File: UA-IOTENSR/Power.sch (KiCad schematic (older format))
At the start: 23 parts, among them IC201 BQ2000TPN-B5, J201 ZX62-AB-5PA_31_, J202 S2B-ZR-SM4A-TF(LF)(SN)

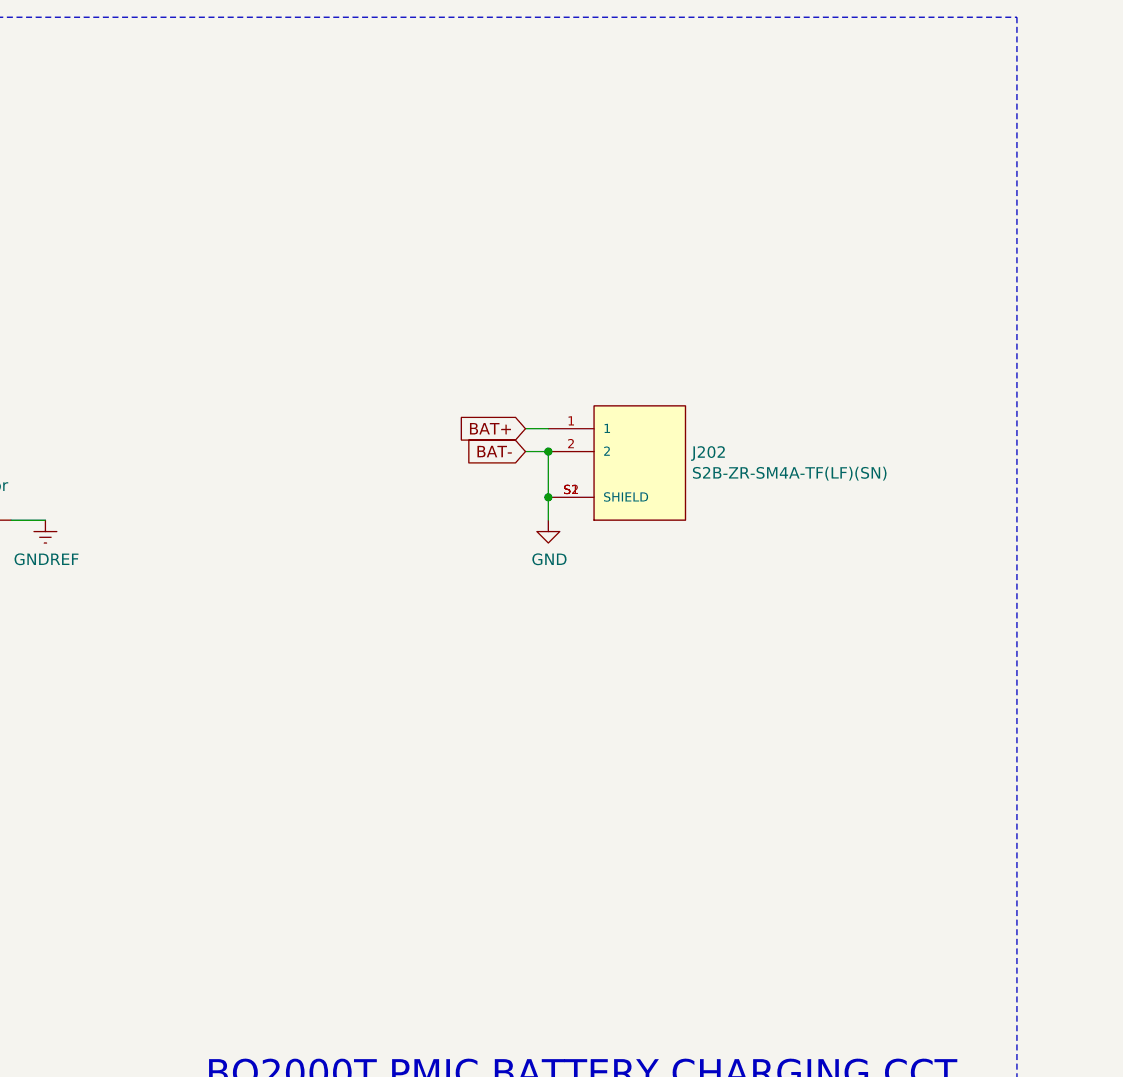
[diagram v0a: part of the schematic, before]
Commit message: Added 3V3 switch reg with footprint
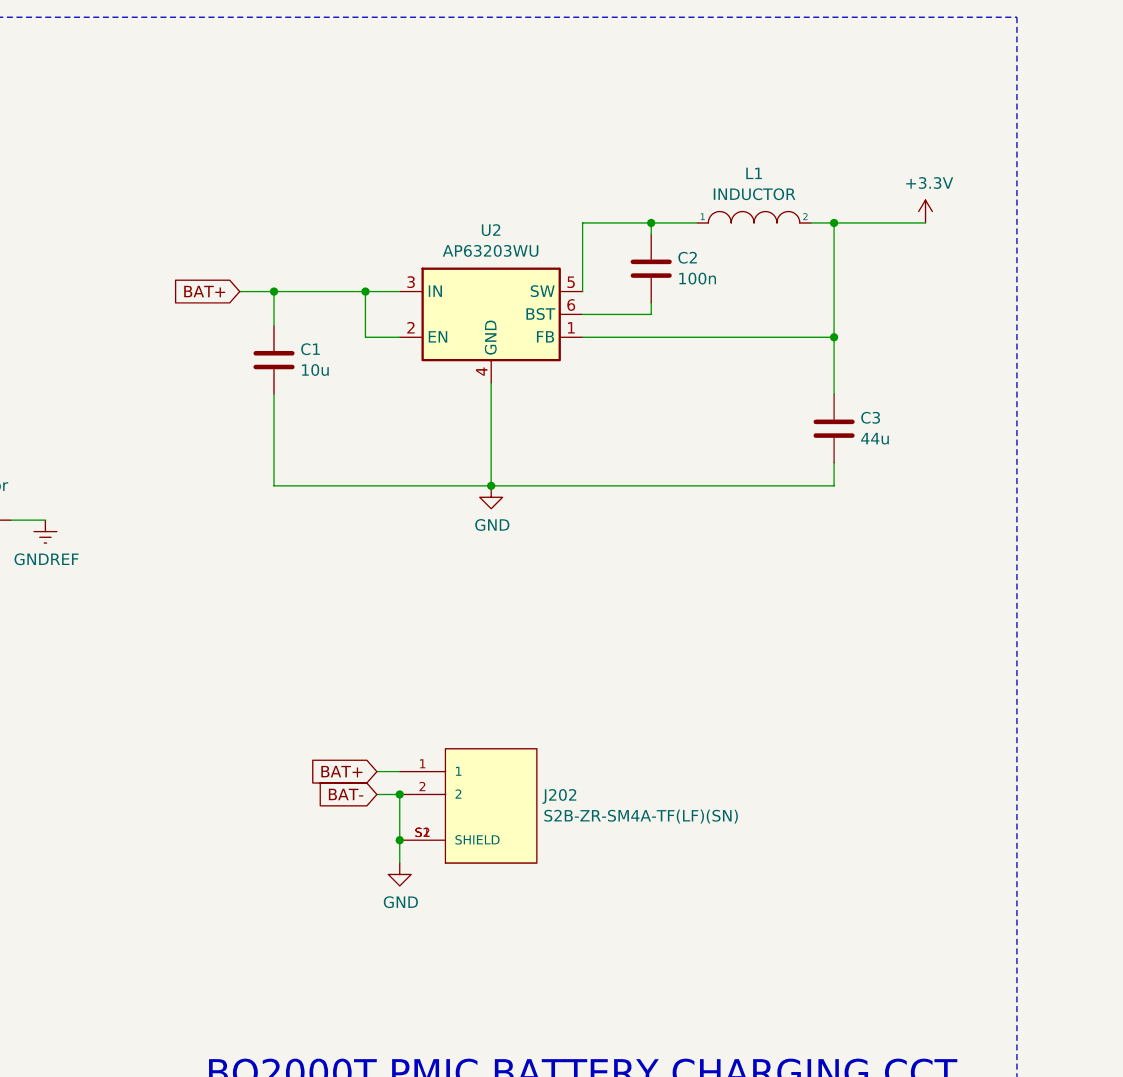
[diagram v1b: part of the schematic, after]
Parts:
- added C1: 10u, Capacitor_SMD:C_0805_2012Metric_Pad1.18x1.45mm_HandSolder, symbol Device:C
- added C2: 100n, Capacitor_SMD:C_0805_2012Metric_Pad1.18x1.45mm_HandSolder, symbol Device:C
- added C3: 44u, Capacitor_SMD:C_0805_2012Metric_Pad1.18x1.45mm_HandSolder, symbol Device:C
- added L1: INDUCTOR, symbol pspice:INDUCTOR
- added U2: AP63203WU, Package_TO_SOT_SMD:TSOT-23-6, symbol Regulator_Switching:AP63203WU
- R208, R209: footprint (none) -> Resistor_SMD:R_0805_2012Metric_Pad1.20x1.40mm_HandSolder
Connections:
- net BAT+: now also C1.1, U2.2 (EN), U2.3 (IN)
- net GND: now also C1.2, C3.2, U2.4 (GND)
- new net: C2.1, L1.1, U2.5 (SW)
- new net: C2.2, U2.6 (BST)
- new net +3V3: C3.1, L1.2, U2.1 (FB)
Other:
- moved on the sheet: J202
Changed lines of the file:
@@
 Text Notes 7000 7100 0    236  ~ 0
 BQ2000T PMIC CCT
-Connection ~ 7950 2600
-Wire Wire Line
-	7950 2400 7950 2600
-Wire Wire Line
-	7950 2600 7950 2700
+Connection ~ 7300 4100
+Wire Wire Line
+	7300 3900 7300 4100
+Wire Wire Line
+	7300 4100 7300 4200
 $Comp
 L JSTConns:S2B-ZR-SM4A-TF(LF)(SN) J202
 U 1 1 619CB2DD
-P 8350 2500
-F 0 "J202" H 8578 2596 50  0000 L CNN
-F 1 "S2B-ZR-SM4A-TF(LF)(SN)" H 8578 2505 50  0000 L CNN
-F 2 "JSTConns:JST_S2B-ZR-SM4A-TF(LF)(SN)" H 8350 2500 50  0001 L BNN
-F 3 "" H 8350 2500 50  0001 L BNN
-F 4 "Manufacturer Recommendations" H 8350 2500 50  0001 L BNN "STANDARD"
-F 5 "JST" H 8350 2500 50  0001 L BNN "MF"
-F 6 "N/A" H 8350 2500 50  0001 L BNN "PARTREV"
-	1    8350 2500
+P 7700 4000
+F 0 "J202" H 7928 4096 50  0000 L CNN
+F 1 "S2B-ZR-SM4A-TF(LF)(SN)" H 7928 4005 50  0000 L CNN
+F 2 "JSTConns:JST_S2B-ZR-SM4A-TF(LF)(SN)" H 7700 4000 50  0001 L BNN
+F 3 "" H 7700 4000 50  0001 L BNN
+F 4 "Manufacturer Recommendations" H 7700 4000 50  0001 L BNN "STANDARD"
+F 5 "JST" H 7700 4000 50  0001 L BNN "MF"
+F 6 "N/A" H 7700 4000 50  0001 L BNN "PARTREV"
+	1    7700 4000
 	1    0    0    -1
 $EndComp
@@
 L power:GND #PWR?
 U 1 1 61A7BC83
-P 7950 2700
+P 7300 4200
 AR Path="/61A7BC83" Ref="#PWR?"  Part="1"
 AR Path="/61A2F8E2/61A7BC83" Ref="#PWR0208"  Part="1"
-F 0 "#PWR0208" H 7950 2450 50  0001 C CNN
-F 1 "GND" H 7955 2527 50  0000 C CNN
-F 2 "" H 7950 2700 50  0001 C CNN
-F 3 "" H 7950 2700 50  0001 C CNN
-	1    7950 2700
+F 0 "#PWR0208" H 7300 3950 50  0001 C CNN
+F 1 "GND" H 7305 4027 50  0000 C CNN
+F 2 "" H 7300 4200 50  0001 C CNN
+F 3 "" H 7300 4200 50  0001 C CNN
+	1    7300 4200
 	1    0    0    -1
 $EndComp
@@
 Connection ~ 4350 3100
 Wire Wire Line
-	7950 2400 7850 2400
-Connection ~ 7950 2400
-Wire Wire Line
-	7950 2300 7850 2300
-Text GLabel 7850 2300 0    50   Input ~ 0
+	7300 3900 7200 3900
+Connection ~ 7300 3900
+Wire Wire Line
+	7300 3800 7200 3800
+Text GLabel 7200 3800 0    50   Input ~ 0
 BAT+
-Text GLabel 7850 2400 0    50   Input ~ 0
+Text GLabel 7200 3900 0    50   Input ~ 0
 BAT-
 Wire Wire Line
@@
 F 0 "R209" H 4968 3046 50  0000 L CNN
 F 1 "5.7668k" H 4968 2955 50  0000 L CNN
-F 2 "" V 4940 2990 50  0001 C CNN
+F 2 "Resistor_SMD:R_0805_2012Metric_Pad1.20x1.40mm_HandSolder" V 4940 2990 50  0001 C CNN
 F 3 "~" H 4900 3000 50  0001 C CNN
 	1    4900 3000
@@
 F 0 "R208" H 4968 2396 50  0000 L CNN
 F 1 "4.8047k" H 4968 2305 50  0000 L CNN
-F 2 "" V 4940 2340 50  0001 C CNN
+F 2 "Resistor_SMD:R_0805_2012Metric_Pad1.20x1.40mm_HandSolder" V 4940 2340 50  0001 C CNN
 F 3 "~" H 4900 2350 50  0001 C CNN
 	1    4900 2350
@@
 Wire Wire Line
 	4900 2500 4900 2700
+$Comp
+L Regulator_Switching:AP63203WU U2
+U 1 1 620AEB9B
+P 7700 1800
+F 0 "U2" H 7700 2167 50  0000 C CNN
+F 1 "AP63203WU" H 7700 2076 50  0000 C CNN
+F 2 "Package_TO_SOT_SMD:TSOT-23-6" H 7700 900 50  0001 C CNN
+F 3 "https://www.diodes.com/assets/Datasheets/AP63200-AP63201-AP63203-AP63205.pdf" H 7700 1800 50  0001 C CNN
+	1    7700 1800
+	1    0    0    -1
+$EndComp
+Wire Wire Line
+	7300 1700 7150 1700
+Text GLabel 6600 1700 0    50   Input ~ 0
+BAT+
+Wire Wire Line
+	6750 1700 6750 1850
+Connection ~ 6750 1700
+Wire Wire Line
+	6750 1700 6600 1700
+Wire Wire Line
+	7150 1700 7150 1900
+Wire Wire Line
+	7150 1900 7300 1900
+Connection ~ 7150 1700
+Wire Wire Line
+	7150 1700 6750 1700
+Wire Wire Line
+	8100 1400 8400 1400
+$Comp
+L Device:C C1
+U 1 1 620C3D23
+P 6750 2000
+F 0 "C1" H 6865 2046 50  0000 L CNN
+F 1 "10u" H 6865 1955 50  0000 L CNN
+F 2 "Capacitor_SMD:C_0805_2012Metric_Pad1.18x1.45mm_HandSolder" H 6788 1850 50  0001 C CNN
+F 3 "~" H 6750 2000 50  0001 C CNN
+	1    6750 2000
+	1    0    0    -1
+$EndComp
+Wire Wire Line
+	8100 1700 8100 1400
+Wire Wire Line
+	8100 1800 8400 1800
+$Comp
+L Device:C C2
+U 1 1 620CB043
+P 8400 1600
+F 0 "C2" H 8515 1646 50  0000 L CNN
+F 1 "100n" H 8515 1555 50  0000 L CNN
+F 2 "Capacitor_SMD:C_0805_2012Metric_Pad1.18x1.45mm_HandSolder" H 8438 1450 50  0001 C CNN
+F 3 "~" H 8400 1600 50  0001 C CNN
+	1    8400 1600
+	1    0    0    -1
+$EndComp
+Wire Wire Line
+	8400 1750 8400 1800
+Wire Wire Line
+	8400 1450 8400 1400
+Connection ~ 8400 1400
+Wire Wire Line
+	8400 1400 8600 1400
+Wire Wire Line
+	7700 2100 7700 2550
+Wire Wire Line
+	6750 2150 6750 2550
+Wire Wire Line
+	6750 2550 7700 2550
+$Comp
+L power:GND #PWR0106
+U 1 1 620D4ECA
+P 7700 2550
+F 0 "#PWR0106" H 7700 2300 50  0001 C CNN
+F 1 "GND" H 7705 2377 50  0000 C CNN
+F 2 "" H 7700 2550 50  0001 C CNN
+F 3 "" H 7700 2550 50  0001 C CNN
+	1    7700 2550
+	1    0    0    -1
+$EndComp
+Connection ~ 7700 2550
+$Comp
+L pspice:INDUCTOR L1
+U 1 1 620D58E6
+P 8850 1400
+F 0 "L1" H 8850 1615 50  0000 C CNN
+F 1 "INDUCTOR" H 8850 1524 50  0000 C CNN
+F 2 "" H 8850 1400 50  0001 C CNN
+F 3 "~" H 8850 1400 50  0001 C CNN
+	1    8850 1400
+	1    0    0    -1
+$EndComp
+Wire Wire Line
+	9200 1900 9200 1400
+Wire Wire Line
+	8100 1900 9200 1900
+Wire Wire Line
+	9100 1400 9200 1400
+$Comp
+L Device:C C3
+U 1 1 620DE76A
+P 9200 2300
+F 0 "C3" H 9315 2346 50  0000 L CNN
+F 1 "44u" H 9315 2255 50  0000 L CNN
+F 2 "Capacitor_SMD:C_0805_2012Metric_Pad1.18x1.45mm_HandSolder" H 9238 2150 50  0001 C CNN
+F 3 "~" H 9200 2300 50  0001 C CNN
+	1    9200 2300
+	1    0    0    -1
+$EndComp
+Connection ~ 9200 1900
+Wire Wire Line
+	9200 1900 9200 2150
+Wire Wire Line
+	9200 2450 9200 2550
+Wire Wire Line
+	9200 2550 7700 2550
+Wire Wire Line
+	9200 1400 9600 1400
+Connection ~ 9200 1400
+$Comp
+L power:+3.3V #PWR0108
+U 1 1 620E9E85
+P 9600 1400
+F 0 "#PWR0108" H 9600 1250 50  0001 C CNN
+F 1 "+3.3V" H 9615 1573 50  0000 C CNN
+F 2 "" H 9600 1400 50  0001 C CNN
+F 3 "" H 9600 1400 50  0001 C CNN
+	1    9600 1400
+	1    0    0    -1
+$EndComp
 $EndSCHEMATC

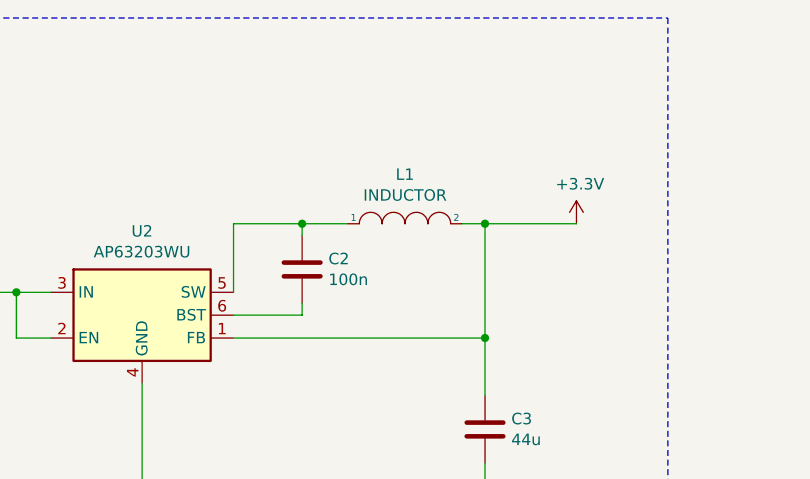
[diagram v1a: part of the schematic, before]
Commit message: Completed regulator circuit; switched to 4-layer board setup
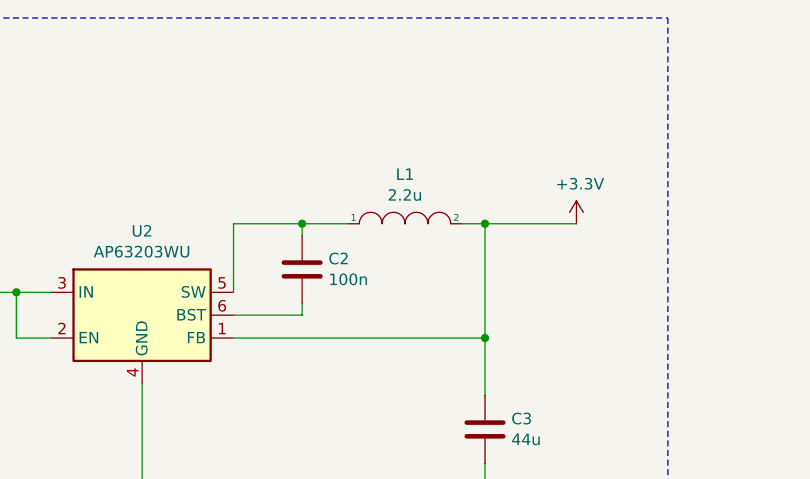
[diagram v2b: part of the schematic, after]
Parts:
- L1: value INDUCTOR -> 2.2u; footprint (none) -> Inductor_SMD:L_0805_2012Metric_Pad1.15x1.40mm_HandSolder
- L201: footprint 30u_inductor:B82559A0303A024 -> Inductor_SMD:L_0805_2012Metric_Pad1.15x1.40mm_HandSolder
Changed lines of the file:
@@
 F 0 "L201" V 3569 3450 50  0000 C CNN
 F 1 "30u" V 3660 3450 50  0000 C CNN
-F 2 "30u_inductor:B82559A0303A024" H 3750 3450 50  0001 C CNN
+F 2 "Inductor_SMD:L_0805_2012Metric_Pad1.15x1.40mm_HandSolder" H 3750 3450 50  0001 C CNN
 F 3 "~" H 3750 3450 50  0001 C CNN
 	1    3750 3450
@@
 P 8850 1400
 F 0 "L1" H 8850 1615 50  0000 C CNN
-F 1 "INDUCTOR" H 8850 1524 50  0000 C CNN
-F 2 "" H 8850 1400 50  0001 C CNN
+F 1 "2.2u" H 8850 1524 50  0000 C CNN
+F 2 "Inductor_SMD:L_0805_2012Metric_Pad1.15x1.40mm_HandSolder" H 8850 1400 50  0001 C CNN
 F 3 "~" H 8850 1400 50  0001 C CNN
 	1    8850 1400

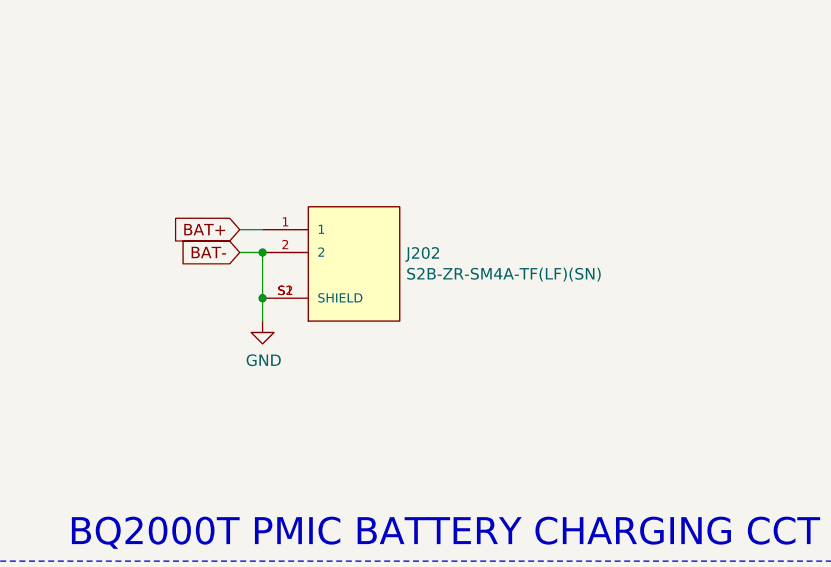
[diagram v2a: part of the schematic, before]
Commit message: Switched JST Conn to Battery Holder 3x AA
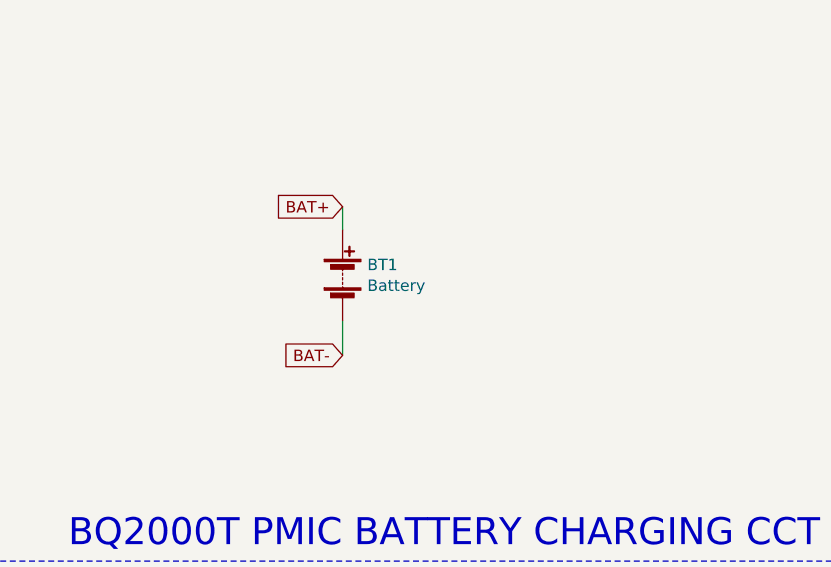
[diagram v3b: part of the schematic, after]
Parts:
- removed J202: S2B-ZR-SM4A-TF(LF)(SN), JSTConns:JST_S2B-ZR-SM4A-TF(LF)(SN), symbol JSTConns:S2B-ZR-SM4A-TF(LF)(SN)
- added BT1: Battery, Battery:BatteryHolder_TruPower_BH-331P_3xAA, symbol Device:Battery
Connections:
- net BAT+: now also BT1.1 (+)
- net GND: now also BT1.2 (-)
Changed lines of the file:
@@
 Text Notes 7000 7100 0    236  ~ 0
 BQ2000T PMIC CCT
-Connection ~ 7300 4100
-Wire Wire Line
-	7300 3900 7300 4100
-Wire Wire Line
-	7300 4100 7300 4200
-$Comp
-L JSTConns:S2B-ZR-SM4A-TF(LF)(SN) J202
-U 1 1 619CB2DD
-P 7700 4000
-F 0 "J202" H 7928 4096 50  0000 L CNN
-F 1 "S2B-ZR-SM4A-TF(LF)(SN)" H 7928 4005 50  0000 L CNN
-F 2 "JSTConns:JST_S2B-ZR-SM4A-TF(LF)(SN)" H 7700 4000 50  0001 L BNN
-F 3 "" H 7700 4000 50  0001 L BNN
-F 4 "Manufacturer Recommendations" H 7700 4000 50  0001 L BNN "STANDARD"
-F 5 "JST" H 7700 4000 50  0001 L BNN "MF"
-F 6 "N/A" H 7700 4000 50  0001 L BNN "PARTREV"
-	1    7700 4000
-	1    0    0    -1
-$EndComp
-$Comp
-L power:GND #PWR?
-U 1 1 61A7BC83
-P 7300 4200
-AR Path="/61A7BC83" Ref="#PWR?"  Part="1"
-AR Path="/61A2F8E2/61A7BC83" Ref="#PWR0208"  Part="1"
-F 0 "#PWR0208" H 7300 3950 50  0001 C CNN
-F 1 "GND" H 7305 4027 50  0000 C CNN
-F 2 "" H 7300 4200 50  0001 C CNN
-F 3 "" H 7300 4200 50  0001 C CNN
-	1    7300 4200
-	1    0    0    -1
-$EndComp
 $Comp
 L UA-IOTENSR-rescue:BQ2000TPN-B5-Samacs IC201
@@
 Connection ~ 4350 3100
 Wire Wire Line
-	7300 3900 7200 3900
-Connection ~ 7300 3900
-Wire Wire Line
-	7300 3800 7200 3800
-Text GLabel 7200 3800 0    50   Input ~ 0
-BAT+
-Text GLabel 7200 3900 0    50   Input ~ 0
-BAT-
-Wire Wire Line
 	4050 1800 4050 1400
 Wire Wire Line
@@
 	1    0    0    -1
 $EndComp
+$Comp
+L Device:Battery BT1
+U 1 1 620B3C7A
+P 7650 4000
+F 0 "BT1" H 7758 4046 50  0000 L CNN
+F 1 "Battery" H 7758 3955 50  0000 L CNN
+F 2 "Battery:BatteryHolder_TruPower_BH-331P_3xAA" V 7650 4060 50  0001 C CNN
+F 3 "~" V 7650 4060 50  0001 C CNN
+	1    7650 4000
+	1    0    0    -1
+$EndComp
+Wire Wire Line
+	7650 3800 7650 3700
+Wire Wire Line
+	7650 4200 7650 4350
+Text GLabel 7650 3700 0    50   Input ~ 0
+BAT+
+Text GLabel 7650 4350 0    50   Input ~ 0
+BAT-
 $EndSCHEMATC
